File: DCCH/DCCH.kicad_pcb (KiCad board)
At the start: 4 copper layers, 139.7 x 88.9 mm, 28 parts, among them J1 Conn_01x02, J2 Conn_01x02, J3 Conn_01x05, J4 Conn_01x05, J5 Conn_01x16, U11 SN74HC595, U12 SN74HC595, U13 SN74HC595, U21 SN754410, U22 SN754410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

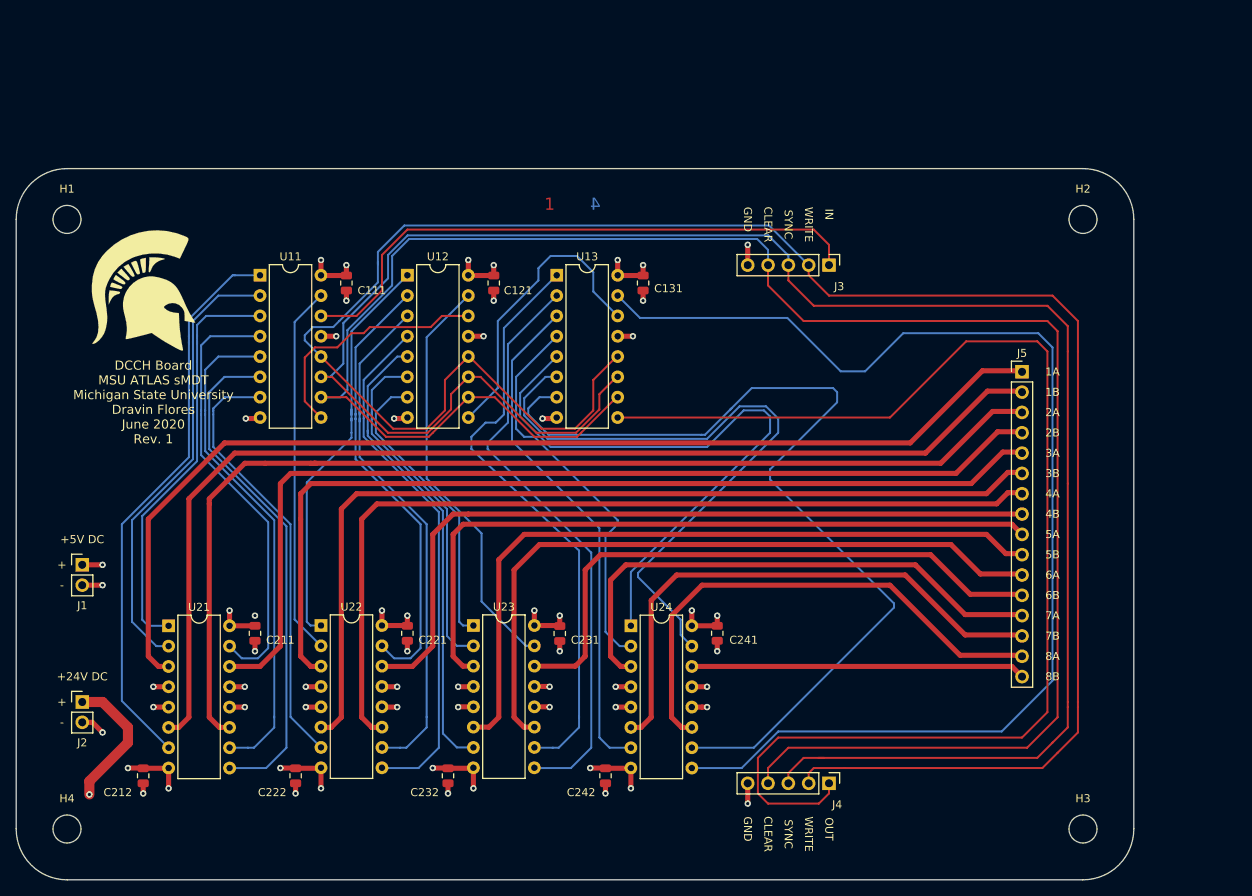
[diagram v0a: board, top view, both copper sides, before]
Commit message: Rewired everything. Removed the resistors. Now the control bit pattern for the shift registers makes sense.
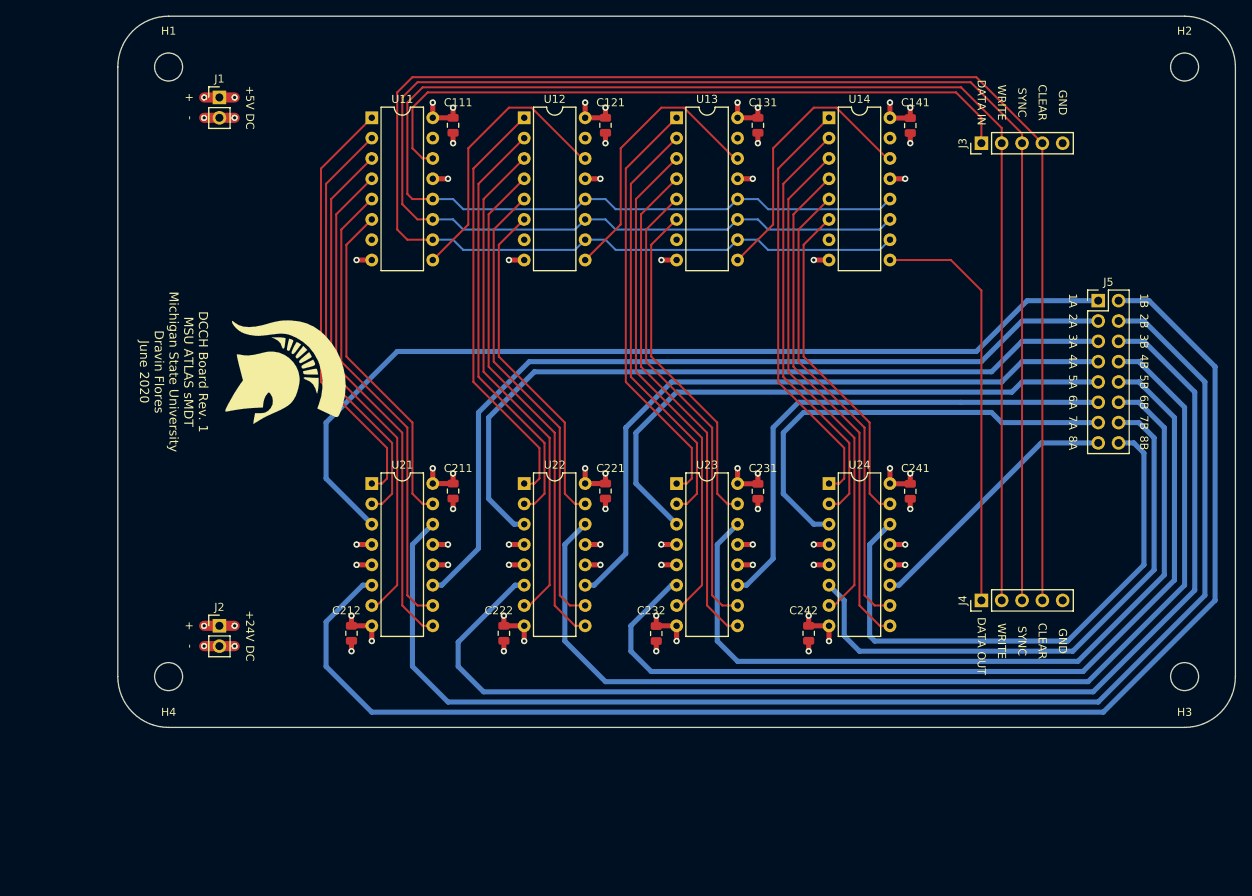
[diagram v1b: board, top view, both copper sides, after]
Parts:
- added C141: 0.1 uF, Capacitor_SMD:C_0805_2012Metric, F.Cu at (168.9, 51.8)
- added U14: SN74HC595, Package_DIP:DIP-16_W7.62mm, F.Cu at (158.8, 50.8)
- J5: value Conn_01x16 -> Conn_02x08_Odd_Even; footprint Connector_PinHeader_2.54mm:PinHeader_1x16_P2.54mm_Vertical -> Connector_PinHeader_2.54mm:PinHeader_2x08_P2.54mm_Vertical
- moved J1 60.9 mm to (82.5, 48.3)
- moved C212 31.5 mm to (99.1, 115.2)
- moved C222 31.5 mm to (118.1, 115.2)
- moved C232 31.5 mm to (137.2, 115.3)
- moved C242 31.0 mm to (156.2, 115.2)
- moved U21 31.0 mm to (101.6, 96.5)
- moved U22 31.0 mm to (120.7, 96.5)
- moved U23 31.0 mm to (139.7, 96.5)
- moved C231 30.5 mm to (149.9, 97.5)
- moved C211 30.5 mm to (111.8, 97.5)
- moved C221 30.5 mm to (130.8, 97.5)
- moved U24 30.5 mm to (158.8, 96.5)
- moved C241 30.0 mm to (168.9, 97.5)
- moved J4 29.8 mm to (177.8, 111.1), turned to 90 degrees
- moved U13 24.7 mm to (139.7, 50.8)
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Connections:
- J4 pad 1: SER-13 -> SER-14
- U11 pad 15: CON-11A -> (no net)
- U11 pad 7: CON-11H -> (no net)
- U12 pad 15: CON-12A -> (no net)
- U12 pad 7: CON-12H -> (no net)
- U13 pad 15: CON-13A -> (no net)
- U13 pad 7: CON-13H -> (no net)
- U21 pad 1: CON-11D -> CON-11B
- U21 pad 15: CON-11E -> CON-11G
- U21 pad 7: CON-11B -> CON-11D
- U21 pad 9: CON-11G -> CON-11E
- U22 pad 10: CON-12D -> CON-12F
- U22 pad 15: CON-12C -> CON-12G
- U22 pad 2: CON-11A -> CON-12C
- U22 pad 7: CON-11H -> CON-12D
- U23 pad 1: CON-12H -> CON-13B
- U23 pad 10: CON-13B -> CON-13F
- U23 pad 15: CON-12A -> CON-13G
- U23 pad 2: CON-12G -> CON-13C
- U23 pad 7: CON-12F -> CON-13D
- U23 pad 9: CON-13C -> CON-13E
- U24 pad 1: CON-13F -> CON-14B
- U24 pad 10: CON-13H -> CON-14F
- U24 pad 15: CON-13G -> CON-14G
- U24 pad 2: CON-13E -> CON-14C
- U24 pad 7: CON-13D -> CON-14D
- U24 pad 9: CON-13A -> CON-14E
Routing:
- net CON-13A: track 152.3 -> 0.00 mm
- net SER-13: track 157.5 -> 35.2 mm
- net CON-13H: track 116.7 -> 0.00 mm
- net CON-14E: track 0.00 -> 63.5 mm
- net CON-14D: track 0.00 -> 63.1 mm
- net CON-14F: track 0.00 -> 58.2 mm
- net CON-11H: track 54.4 -> 0.00 mm
- net CON-14B: track 0.00 -> 53.3 mm
- net CON-14C: track 0.00 -> 53.3 mm
- net CON-12A: track 52.1 -> 0.00 mm
- net SER-14: track 0.00 -> 51.7 mm
- net WRITE: track 258.7 -> 211.4 mm
- net CON-11A: track 46.5 -> 0.00 mm
- net OUT-2B: track 123.2 -> 165.9 mm
- net CON-14G: track 0.00 -> 42.1 mm
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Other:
- outline, holes or cut-outs redrawn
- board text added: "DATA IN"
- board text added: "DATA OUT"
- board text added: "DCCH Board Rev. 1 MSU ATLAS sMDT Michigan State University Dravin Flores June 2020"
- board text removed: "1"
- board text removed: "2"
- board text removed: "3"
- board text removed: "4"
- board text removed: "DCCH Board MSU ATLAS sMDT Michigan State University Dravin Flores June 2020 Rev. 1"
- board text removed: "IN"
- board text removed: "LAYER"
- board text removed: "OUT"
- board text removed: "Switching Signal Bus."

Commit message: Removed the vias from the power connectors.
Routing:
- net GND: track 68.8 -> 61.2 mm, vias 40 -> 36
- net +5V: track 49.7 -> 45.8 mm, vias 18 -> 16
- net +24V: track 26.7 -> 22.9 mm, vias 10 -> 8

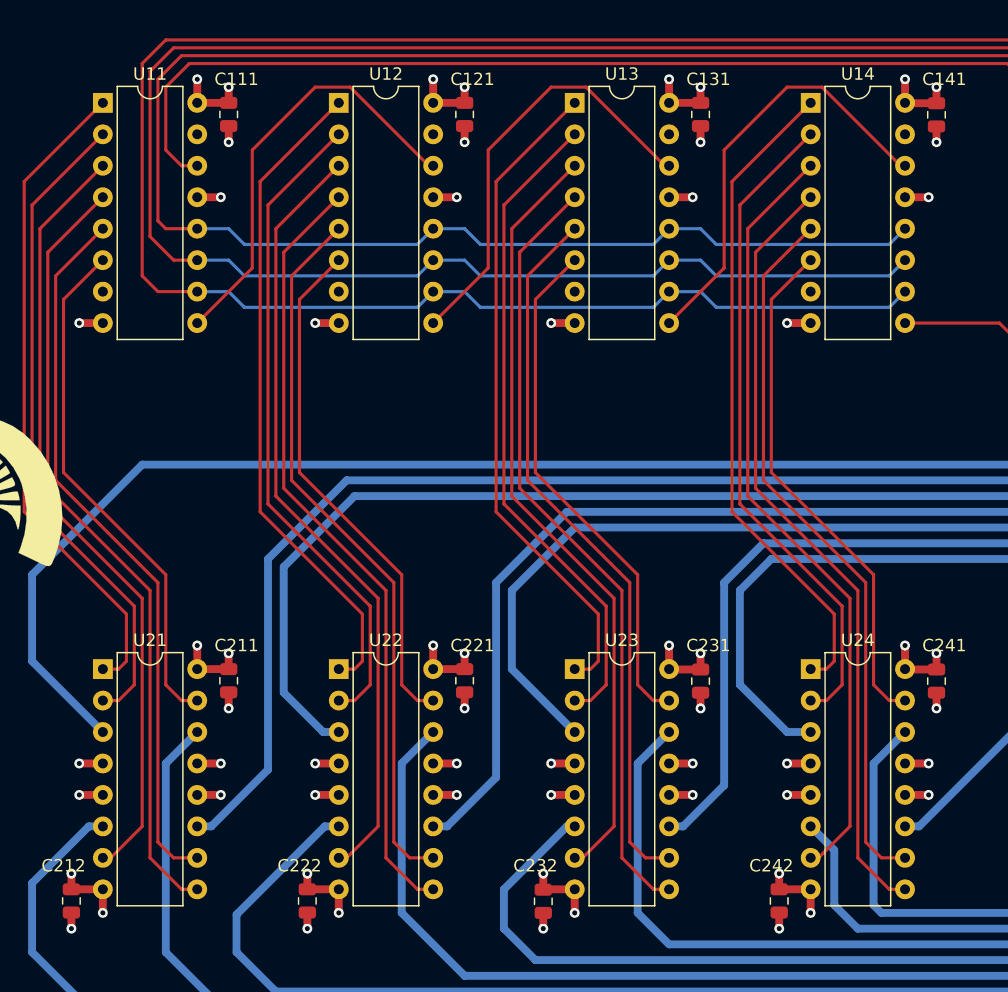
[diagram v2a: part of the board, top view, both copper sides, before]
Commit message: Removed power traces and vias. Power plane connects these nets automatically.
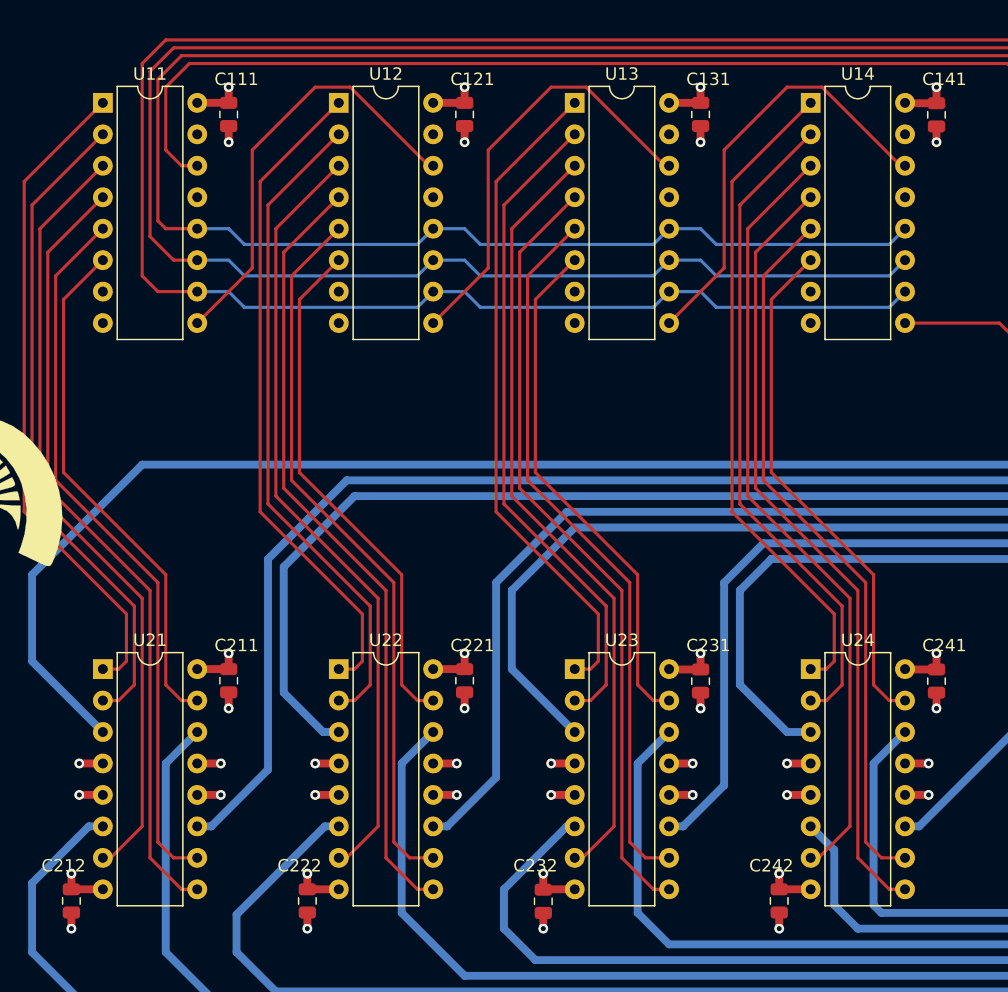
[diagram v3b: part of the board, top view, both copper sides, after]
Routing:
- net GND: track 61.2 -> 46.0 mm, vias 36 -> 28
- net +5V: track 45.8 -> 30.6 mm, vias 16 -> 8
- net +24V: track 22.9 -> 15.3 mm, vias 8 -> 4
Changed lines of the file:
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@@
     (thickness 1.6)
     (drawings 67)
-    (tracks 483)
+    (tracks 443)
     (zones 0)
     (modules 30)
@@
     (0 SIG-1 signal)
     (1 PWR power)
-    (2 GND power hide)
+    (2 GND power)
     (31 SIG-2 signal)
     (33 F.Adhes user)
@@
   (via (at 99.06 117.475) (size 0.8) (drill 0.4) (layers SIG-1 SIG-2) (net 1))
   (via (at 168.91 53.975) (size 0.8) (drill 0.4) (layers SIG-1 SIG-2) (net 1))
-  (via (at 168.275 58.42) (size 0.8) (drill 0.4) (layers SIG-1 SIG-2) (net 1))
-  (via (at 156.845 68.58) (size 0.8) (drill 0.4) (layers SIG-1 SIG-2) (net 1))
   (via (at 149.86 53.975) (size 0.8) (drill 0.4) (layers SIG-1 SIG-2) (net 1))
   (via (at 130.81 53.975) (size 0.8) (drill 0.4) (layers SIG-1 SIG-2) (net 1))
-  (via (at 149.225 58.42) (size 0.8) (drill 0.4) (layers SIG-1 SIG-2) (net 1))
-  (via (at 137.795 68.58) (size 0.8) (drill 0.4) (layers SIG-1 SIG-2) (net 1))
-  (via (at 130.175 58.42) (size 0.8) (drill 0.4) (layers SIG-1 SIG-2) (net 1))
-  (via (at 118.745 68.58) (size 0.8) (drill 0.4) (layers SIG-1 SIG-2) (net 1))
-  (via (at 99.695 68.58) (size 0.8) (drill 0.4) (layers SIG-1 SIG-2) (net 1))
-  (via (at 111.125 58.42) (size 0.8) (drill 0.4) (layers SIG-1 SIG-2) (net 1))
   (via (at 111.76 53.975) (size 0.8) (drill 0.4) (layers SIG-1 SIG-2) (net 1))
-  (segment (start 99.695 68.58) (end 101.6 68.58) (width 0.635) (layer SIG-1) (net 1))
-  (segment (start 109.22 58.42) (end 111.125 58.42) (width 0.635) (layer SIG-1) (net 1))
   (segment (start 111.76 53.975) (end 111.76 52.675) (width 0.635) (layer SIG-1) (net 1))
   (segment (start 130.81 53.975) (end 130.81 52.675) (width 0.635) (layer SIG-1) (net 1))
-  (segment (start 128.27 58.42) (end 130.175 58.42) (width 0.635) (layer SIG-1) (net 1))
-  (segment (start 118.745 68.58) (end 120.65 68.58) (width 0.635) (layer SIG-1) (net 1))
-  (segment (start 137.795 68.58) (end 139.7 68.58) (width 0.635) (layer SIG-1) (net 1))
-  (segment (start 147.32 58.42) (end 149.225 58.42) (width 0.635) (layer SIG-1) (net 1))
   (segment (start 149.86 53.975) (end 149.86 52.675) (width 0.635) (layer SIG-1) (net 1))
-  (segment (start 156.845 68.58) (end 158.75 68.58) (width 0.635) (layer SIG-1) (net 1))
-  (segment (start 166.37 58.42) (end 168.275 58.42) (width 0.635) (layer SIG-1) (net 1))
   (segment (start 168.91 52.705) (end 168.91 53.975) (width 0.635) (layer SIG-1) (net 1))
   (segment (start 99.06 117.475) (end 99.06 116.175) (width 0.635) (layer SIG-1) (net 1))
@@
   (segment (start 168.91 99.695) (end 168.91 98.425) (width 0.635) (layer SIG-1) (net 1))
   (via (at 111.76 49.53) (size 0.8) (drill 0.4) (layers SIG-1 SIG-2) (net 2))
-  (via (at 109.22 48.895) (size 0.8) (drill 0.4) (layers SIG-1 SIG-2) (net 2))
-  (via (at 128.27 48.895) (size 0.8) (drill 0.4) (layers SIG-1 SIG-2) (net 2))
   (via (at 130.81 49.53) (size 0.8) (drill 0.4) (layers SIG-1 SIG-2) (net 2))
-  (via (at 147.32 48.895) (size 0.8) (drill 0.4) (layers SIG-1 SIG-2) (net 2))
   (via (at 149.86 49.53) (size 0.8) (drill 0.4) (layers SIG-1 SIG-2) (net 2))
-  (via (at 166.37 48.895) (size 0.8) (drill 0.4) (layers SIG-1 SIG-2) (net 2))
   (via (at 168.91 49.53) (size 0.8) (drill 0.4) (layers SIG-1 SIG-2) (net 2))
-  (via (at 166.37 94.615) (size 0.8) (drill 0.4) (layers SIG-1 SIG-2) (net 2))
   (via (at 168.91 95.25) (size 0.8) (drill 0.4) (layers SIG-1 SIG-2) (net 2))
-  (via (at 147.32 94.615) (size 0.8) (drill 0.4) (layers SIG-1 SIG-2) (net 2))
   (via (at 149.86 95.25) (size 0.8) (drill 0.4) (layers SIG-1 SIG-2) (net 2))
-  (via (at 128.27 94.615) (size 0.8) (drill 0.4) (layers SIG-1 SIG-2) (net 2))
   (via (at 130.81 95.25) (size 0.8) (drill 0.4) (layers SIG-1 SIG-2) (net 2))
   (via (at 111.76 95.25) (size 0.8) (drill 0.4) (layers SIG-1 SIG-2) (net 2))
-  (via (at 109.22 94.615) (size 0.8) (drill 0.4) (layers SIG-1 SIG-2) (net 2))
-  (segment (start 109.22 48.895) (end 109.22 50.8) (width 0.635) (layer SIG-1) (net 2))
   (segment (start 111.76 49.53) (end 111.76 50.8) (width 0.635) (layer SIG-1) (net 2))
   (segment (start 111.76 50.8) (end 109.22 50.8) (width 0.635) (layer SIG-1) (net 2))
-  (segment (start 128.27 48.895) (end 128.27 50.8) (width 0.635) (layer SIG-1) (net 2))
   (segment (start 130.81 49.53) (end 130.81 50.8) (width 0.635) (layer SIG-1) (net 2))
   (segment (start 130.81 50.8) (end 128.27 50.8) (width 0.635) (layer SIG-1) (net 2))
-  (segment (start 147.32 48.895) (end 147.32 50.8) (width 0.635) (layer SIG-1) (net 2))
   (segment (start 149.86 49.53) (end 149.86 50.8) (width 0.635) (layer SIG-1) (net 2))
   (segment (start 149.86 50.8) (end 147.32 50.8) (width 0.635) (layer SIG-1) (net 2))
-  (segment (start 166.37 48.895) (end 166.37 50.8) (width 0.635) (layer SIG-1) (net 2))
   (segment (start 168.91 49.53) (end 168.91 50.83) (width 0.635) (layer SIG-1) (net 2))
   (segment (start 166.4 50.83) (end 166.37 50.8) (width 0.635) (layer SIG-1) (net 2))
   (segment (start 168.91 50.83) (end 166.4 50.83) (width 0.635) (layer SIG-1) (net 2))
   (segment (start 168.91 95.25) (end 168.91 96.55) (width 0.635) (layer SIG-1) (net 2))
-  (segment (start 166.37 94.615) (end 166.37 96.52) (width 0.635) (layer SIG-1) (net 2))
   (segment (start 166.4 96.55) (end 166.37 96.52) (width 0.635) (layer SIG-1) (net 2))
   (segment (start 168.91 96.55) (end 166.4 96.55) (width 0.635) (layer SIG-1) (net 2))
   (segment (start 149.86 95.25) (end 149.86 96.55) (width 0.635) (layer SIG-1) (net 2))
-  (segment (start 147.32 94.615) (end 147.32 96.52) (width 0.635) (layer SIG-1) (net 2))
   (segment (start 147.35 96.55) (end 147.32 96.52) (width 0.635) (layer SIG-1) (net 2))
   (segment (start 149.86 96.55) (end 147.35 96.55) (width 0.635) (layer SIG-1) (net 2))
   (segment (start 130.81 95.25) (end 130.81 96.52) (width 0.635) (layer SIG-1) (net 2))
-  (segment (start 128.27 94.615) (end 128.27 96.52) (width 0.635) (layer SIG-1) (net 2))
   (segment (start 130.81 96.52) (end 128.27 96.52) (width 0.635) (layer SIG-1) (net 2))
   (segment (start 111.76 95.25) (end 111.76 96.52) (width 0.635) (layer SIG-1) (net 2))
-  (segment (start 109.22 94.615) (end 109.22 96.52) (width 0.635) (layer SIG-1) (net 2))
   (segment (start 111.76 96.52) (end 109.22 96.52) (width 0.635) (layer SIG-1) (net 2))
   (via (at 99.06 113.03) (size 0.8) (drill 0.4) (layers SIG-1 SIG-2) (net 3))
@@
   (via (at 137.16 113.03) (size 0.8) (drill 0.4) (layers SIG-1 SIG-2) (net 3))
   (via (at 156.21 113.03) (size 0.8) (drill 0.4) (layers SIG-1 SIG-2) (net 3))
-  (via (at 158.75 116.205) (size 0.8) (drill 0.4) (layers SIG-1 SIG-2) (net 3))
-  (via (at 139.7 116.205) (size 0.8) (drill 0.4) (layers SIG-1 SIG-2) (net 3))
-  (via (at 120.65 116.205) (size 0.8) (drill 0.4) (layers SIG-1 SIG-2) (net 3))
-  (via (at 101.6 116.205) (size 0.8) (drill 0.4) (layers SIG-1 SIG-2) (net 3))
   (segment (start 99.06 113.03) (end 99.06 114.3) (width 0.635) (layer SIG-1) (net 3))
-  (segment (start 101.6 114.3) (end 101.6 116.205) (width 0.635) (layer SIG-1) (net 3))
   (segment (start 118.11 113.03) (end 118.11 114.3) (width 0.635) (layer SIG-1) (net 3))
-  (segment (start 120.65 114.3) (end 120.65 116.205) (width 0.635) (layer SIG-1) (net 3))
   (segment (start 99.06 114.3) (end 101.6 114.3) (width 0.635) (layer SIG-1) (net 3))
   (segment (start 118.11 114.3) (end 120.65 114.3) (width 0.635) (layer SIG-1) (net 3))
   (segment (start 137.16 113.03) (end 137.16 114.33) (width 0.635) (layer SIG-1) (net 3))
-  (segment (start 139.7 114.3) (end 139.7 116.205) (width 0.635) (layer SIG-1) (net 3))
   (segment (start 137.19 114.3) (end 137.16 114.33) (width 0.635) (layer SIG-1) (net 3))
   (segment (start 139.7 114.3) (end 137.19 114.3) (width 0.635) (layer SIG-1) (net 3))
   (segment (start 156.21 113.03) (end 156.21 114.3) (width 0.635) (layer SIG-1) (net 3))
-  (segment (start 158.75 114.3) (end 158.75 116.205) (width 0.635) (layer SIG-1) (net 3))
   (segment (start 158.75 114.3) (end 156.21 114.3) (width 0.635) (layer SIG-1) (net 3))
   (segment (start 177.8 50.8) (end 177.8 53.975) (width 0.254) (layer SIG-1) (net 4))
@@
     (connect_pads (clearance 0.508))
     (min_thickness 0.254)
-    (fill yes (arc_segments 32) (thermal_gap 0.508) (thermal_bridge_width 0.508))
+    (fill yes (arc_segments 32) (thermal_gap 0.508) (thermal_bridge_width 0.635))
     (polygon
       (pts
@@
     (connect_pads (clearance 0.508))
     (min_thickness 0.254)
-    (fill yes (arc_segments 32) (thermal_gap 0.508) (thermal_bridge_width 0.508))
+    (fill yes (arc_segments 32) (thermal_gap 0.508) (thermal_bridge_width 0.635))
     (polygon
       (pts
